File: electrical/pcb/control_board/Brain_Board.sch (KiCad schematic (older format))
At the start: 41 parts, among them J22 S9175-ND_rpi_breakout, J23 S9175-ND_rpi_breakout, J24 6posheader, J25 SSW-104-01-F-T, J26 WM6548-ND, J27 PPTC021LFBN-RC, J28 PPTC021LFBN-RC, J29 PPTC021LFBN-RC, J30 PEC08SAAN, M1 Mounting_Holes, Q2 2N3906, Q3 2N3906, SW1 CT206124-ND, T13 test_point, T14 test_point, T15 test_point, U6 DC7G3HWA

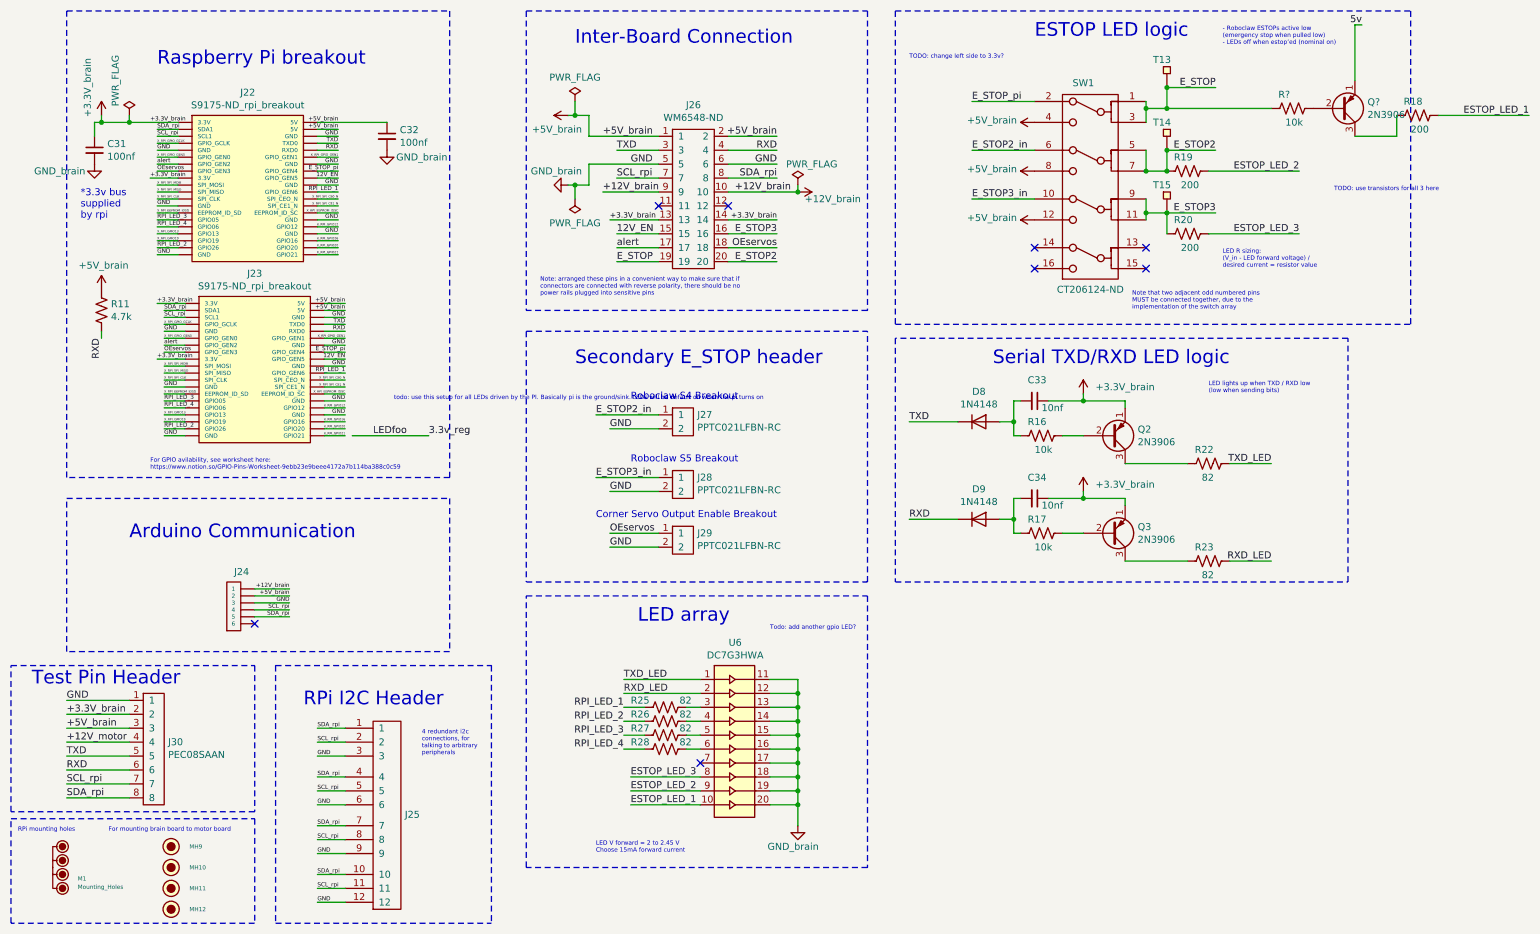
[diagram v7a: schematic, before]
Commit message: Overhauled 3.3v rail and updated LEDs to use it
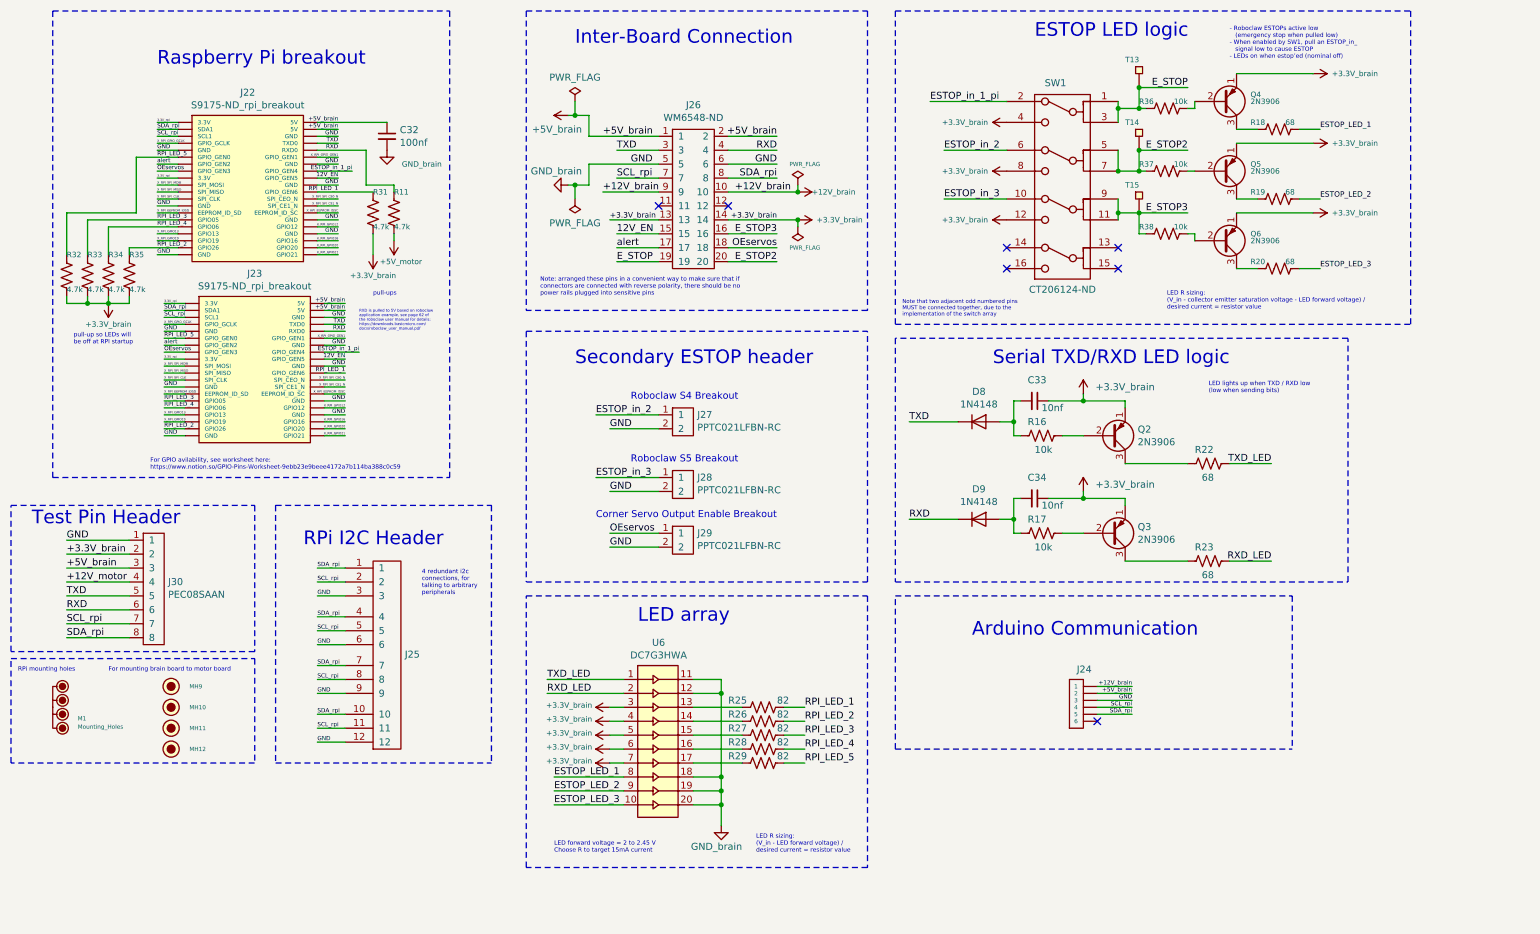
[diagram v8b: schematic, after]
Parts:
- removed C31: 100nf, Resistor_THT:R_Axial_DIN0207_L6.3mm_D2.5mm_P7.62mm_Horizontal, symbol Device:C_Small
- added Q5, Q6: 2N3906, Package_TO_SOT_THT:TO-92_Inline, symbol Transistor_BJT:2N3906
- added R29: 82, Resistor_THT:R_Axial_DIN0207_L6.3mm_D2.5mm_P7.62mm_Horizontal, symbol Device:R_US
- added R31, R32, R33, R34, R35: 4.7k, Resistor_THT:R_Axial_DIN0207_L6.3mm_D2.5mm_P7.62mm_Horizontal, symbol Device:R_US
- added R37, R38: 10k, Resistor_THT:R_Axial_DIN0207_L6.3mm_D2.5mm_P7.62mm_Horizontal, symbol Device:R_US
- R18, R19, R20: value 200 -> 68
- R22, R23: value 82 -> 68
- gave numbers to parts that had none: 2
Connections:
- net 5v is gone; now on net +3.3V_brain: Q4.1 (E)
- net +3.3V_brain: now also SW1.12 (out3_2), SW1.4 (out1_2), SW1.8 (out2_2), U6.3, U6.4, U6.5, U6.6, U6.7, Q5.1 (E), Q6.1 (E), R31.2, R32.2, R33.2, R34.2, R35.2; no longer J22.1 (3.3V), J22.17 (3.3V), J23.1 (3.3V), J23.17 (3.3V)
- net +5V_brain: no longer R11.1, SW1.12 (out3_2), SW1.4 (out1_2), SW1.8 (out2_2)
- net ESTOP_LED_1: now also U6.8; no longer U6.10
- net ESTOP_LED_3: now also U6.10; no longer U6.8
- net E_STOP2: now also R37.2; no longer R19.2
- net E_STOP3: now also R38.2; no longer R20.2
- net GND_brain: no longer U6.13, U6.14, U6.15, U6.16, U6.17
- net RPI_LED_1: now also R25.1, R31.1; no longer R25.2
- net RPI_LED_2: now also R26.1, R35.1; no longer R26.2
- net RPI_LED_3: now also R27.1, R33.1; no longer R27.2
- net RPI_LED_4: now also R28.1, R34.1; no longer R28.2
- net RXD: now also R11.1; no longer R11.2
- net E_STOP2_in renamed ESTOP_in_2
- net E_STOP3_in renamed ESTOP_in_3
- net E_STOP_pi renamed ESTOP_in_1_pi
- net X_RPI_GPIO_GEN0 renamed RPI_LED_5
- net RPI_LED_5: now also R29.1, R32.1
- new net: R25.2, U6.13
- new net: R26.2, U6.14
- new net: R27.2, U6.15
- new net: R28.2, U6.16
- new net: R29.2, U6.17
- new net: Q5.2 (B), R37.1
- new net: Q5.3 (C), R19.2
- new net: Q6.2 (B), R38.1
- new net: Q6.3 (C), R20.2
- new net +5V_motor: R11.2
- new net 3.3V_rpi: J22.1 (3.3V), J22.17 (3.3V), J23.1 (3.3V), J23.17 (3.3V)
- no-connect marks 8 -> 7
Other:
- note added: "- Roboclaw ESTOPs active low \n (emergency stop when pulled low)\n- When enabled by SW1, pull an ESTOP_in_ \n signal low to cause ESTOP\n- LEDs on when estop’ed (nominal off)"
- note added: "LED R sizing: \n(V_in - collector emitter saturation voltage - LED forward voltage) / \ndesired current = resistor value"
- note added: "LED forward voltage = 2 to 2.45 V\nChoose R to target 15mA current"
- note added: "RXD is pulled to 5V based on roboclaw \napplication example, see page 62 of \nthe roboclaw user manual for details: \nhttps://downloads.basicmicro.com/\ndocs/roboclaw_user_manual.pdf"
- note added: "Secondary ESTOP header"
- note added: "pull-up so LEDs will \nbe off at RPI startup"
- note added: "pull-ups"
- note removed: "*3.3v bus \nsupplied\nby rpi"
- note removed: "- Roboclaw ESTOPs active low \n(emergency stop when pulled low)\n- LEDs off when estop’ed (nominal on)"
- note removed: "LED V forward = 2 to 2.45 V\nChoose 15mA forward current"
- note removed: "Secondary E_STOP header"
- note removed: "TODO: change left side to 3.3v?"
- note removed: "TODO: use transistors for all 3 here"
- note removed: "Todo: add another gpio LED?"
- note removed: "todo: use this setup for all LEDs driven by the PI. Basically pi is the ground/sink. LEDs will be default on when the pi turns on"
- moved on the sheet: J24, J25, J30, M1, MH10, MH11, MH12, MH9, Q4, R18, R25, R26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
